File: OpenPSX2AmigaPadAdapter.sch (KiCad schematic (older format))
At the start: 26 parts, among them J1 TO_PS_PAD, J2 TO_AMI, J3 CONN_FTDI, J4 CONN_ICSP, Q1 BSS138, Q2 BSS138, Q3 BSS138, Q4 BSS138, U1 ATMEGA328P-AU, U2 LM1117-3.3, Y1 16Mhz

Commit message: Minor improvements
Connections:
- wire segments 140 -> 116

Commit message: Add cap for ATmega decoupling
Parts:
- added C2: 100n, symbol C
- renumbered C2 to C3, C3 to C6
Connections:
- wire segments 116 -> 118
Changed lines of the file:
@@
 $EndComp
 $Comp
-L C C2
+L C C3
 U 1 1 5D18D235
 P 3200 5450
-F 0 "C2" H 3225 5550 50  0000 L CNN
+F 0 "C3" H 3225 5550 50  0000 L CNN
 F 1 "10u" H 3225 5350 50  0000 L CNN
 F 2 "" H 3238 5300 50  0001 C CNN
@@
 	2000 5000 2000 5300
 Wire Wire Line
-	2000 5150 2300 5150
+	1650 5150 2300 5150
 Wire Wire Line
 	2600 5450 2600 5950
@@
 	2000 5600 2000 5800
 Wire Wire Line
-	2000 5800 3200 5800
+	1650 5800 3200 5800
 Wire Wire Line
 	3200 5800 3200 5600
@@
 	3200 2750 3950 2750
 $Comp
-L C_Small C3
+L C_Small C6
 U 1 1 5D197DBF
 P 4050 2750
-F 0 "C3" H 4060 2820 50  0000 L CNN
+F 0 "C6" H 4060 2820 50  0000 L CNN
 F 1 "100n" H 4060 2670 50  0000 L CNN
 F 2 "Capacitors_SMD:C_0805_HandSoldering" H 4050 2750 50  0001 C CNN
@@
 Wire Wire Line
 	9900 800  9900 900
+$Comp
+L C C2
+U 1 1 5D1A1AA9
+P 1650 5450
+F 0 "C2" H 1675 5550 50  0000 L CNN
+F 1 "100n" H 1675 5350 50  0000 L CNN
+F 2 "" H 1688 5300 50  0001 C CNN
+F 3 "" H 1650 5450 50  0001 C CNN
+	1    1650 5450
+	1    0    0    -1
+$EndComp
+Wire Wire Line
+	1650 5150 1650 5300
+Wire Wire Line
+	1650 5600 1650 5800
+Connection ~ 2000 5800
 $EndSCHEMATC

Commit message: Port to KiCad 5
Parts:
- removed C1, C3: 10u, symbol C
- removed C2: 100n, symbol C
- removed C4, C5: 22p, symbol C
- removed C6: 100n, Capacitors_SMD:C_0805_HandSoldering, symbol C_Small
- removed J1: TO_PS_PAD, symbol CONN_01X09
- removed J2: TO_AMI, symbol DB9_FEMALE_MountingHoles
- removed J3: CONN_FTDI, symbol CONN_01X06
- removed J4: CONN_ICSP, Pin_Headers:Pin_Header_Straight_2x03, symbol CONN_02X03
- removed Q1, Q2, Q3, Q4: BSS138, TO_SOT_Packages_SMD:SOT-23, symbol BSS138
- removed R1: 10k, Resistors_SMD:R_0805_HandSoldering, symbol R
- removed R10: 100, symbol R
- removed R2, R3, R4, R5, R6, R7, R8, R9: 10k, symbol R
- removed U1: ATMEGA328P-AU, TQFP32, symbol ATMEGA328P-AU
- removed U2: LM1117-3.3, symbol LM1117-3.3
- removed Y1: 16Mhz, symbol Crystal
- added C1, C2: 10u, Capacitor_SMD:C_1206_3216Metric_Pad1.42x1.75mm_HandSolder, symbol Device:C
- added C3, C4, C5, C8: 100n, Capacitor_SMD:C_0805_2012Metric_Pad1.15x1.40mm_HandSolder, symbol Device:C
- added C6, C7: 22p, Capacitor_SMD:C_0805_2012Metric_Pad1.15x1.40mm_HandSolder, symbol Device:C
- added D1, D2: LED, LED_SMD:LED_0805_2012Metric_Pad1.15x1.40mm_HandSolder, symbol Device:LED
- added J1: TO_PSX_PAD, Connector_PinHeader_2.54mm:PinHeader_1x09_P2.54mm_Horizontal, symbol Connector:Conn_01x09_Female
- added J2: TO_AMI, w_conn_d-sub:DB_9F, symbol Connector:DB9_Female_MountingHoles
- added J3: CONN_FTDI, Connector_PinSocket_2.54mm:PinSocket_1x06_P2.54mm_Vertical, symbol Connector:Conn_01x06_Male
- added J4: CONN_ICSP, Connector_PinSocket_2.54mm:PinSocket_2x03_P2.54mm_Vertical, symbol Connector_Generic:Conn_02x03_Odd_Even
- added Q1, Q2, Q3, Q4: BSS138, Package_TO_SOT_SMD:SOT-23, symbol Transistor_FET:BSS138
- added R1, R2, R3, R4, R5, R6, R7, R8, R9: 10k, Resistor_SMD:R_0805_2012Metric_Pad1.15x1.40mm_HandSolder, symbol Device:R
- added R10: 100, Resistor_SMD:R_0805_2012Metric_Pad1.15x1.40mm_HandSolder, symbol Device:R
- added R11: 220, Resistor_SMD:R_0805_2012Metric_Pad1.15x1.40mm_HandSolder, symbol Device:R
- added R220: R, Resistor_SMD:R_0805_2012Metric_Pad1.15x1.40mm_HandSolder, symbol Device:R
- added U1: ATmega328P-AU, Package_QFP:TQFP-32_7x7mm_P0.8mm, symbol MCU_Microchip_ATmega:ATmega328P-AU
- added U2: LM1117-3.3, Package_TO_SOT_SMD:SOT-223-3_TabPin2, symbol Regulator_Linear:LM1117-3.3
- added Y1: 16MHz, Crystal:Crystal_HC49-U_Vertical, symbol Device:Crystal
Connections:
- net labels added: led1, led2
- wire segments 118 -> 159
- no-connect marks 7 -> 11
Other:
- note added: "BOTH 10uF CAPS MUST\nPOSSIBLY BE TANTALUM"
- note removed: "BOTH CAPS MUST\nPOSSIBLY BE TANTALUM"

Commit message: Begin working on PCB
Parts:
- J1: footprint Connector_PinHeader_2.54mm:PinHeader_1x09_P2.54mm_Horizontal -> OpenPSX2AmigaPadAdapter:PSX_Pad_Connector
- J3: footprint Connector_PinSocket_2.54mm:PinSocket_1x06_P2.54mm_Vertical -> Connector_PinHeader_2.54mm:PinHeader_1x06_P2.54mm_Vertical
- J4: footprint Connector_PinSocket_2.54mm:PinSocket_2x03_P2.54mm_Vertical -> Connector_PinHeader_2.54mm:PinHeader_2x03_P2.54mm_Vertical
- R12: renamed from R220; value R -> 220
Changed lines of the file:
@@
 $EndComp
 Text Label 6600 7000 2    60   ~ 0
-miso
+mosi
 Text Label 5300 7100 0    60   ~ 0
 reset
@@
 F 0 "J1" H 9728 4826 50  0000 L CNN
 F 1 "TO_PSX_PAD" H 9728 4735 50  0000 L CNN
-F 2 "Connector_PinHeader_2.54mm:PinHeader_1x09_P2.54mm_Horizontal" H 9700 4800 50  0001 C CNN
+F 2 "OpenPSX2AmigaPadAdapter:PSX_Pad_Connector" H 9700 4800 50  0001 C CNN
 F 3 "~" H 9700 4800 50  0001 C CNN
 	1    9700 4800
@@
 F 0 "J4" H 5950 7317 50  0000 C CNN
 F 1 "CONN_ICSP" H 5950 7226 50  0000 C CNN
-F 2 "Connector_PinSocket_2.54mm:PinSocket_2x03_P2.54mm_Vertical" H 5900 7000 50  0001 C CNN
+F 2 "Connector_PinHeader_2.54mm:PinHeader_2x03_P2.54mm_Vertical" H 5900 7000 50  0001 C CNN
 F 3 "~" H 5900 7000 50  0001 C CNN
 	1    5900 7000
@@
 F 0 "J3" H 4008 7331 50  0000 C CNN
 F 1 "CONN_FTDI" H 4008 7240 50  0000 C CNN
-F 2 "Connector_PinSocket_2.54mm:PinSocket_1x06_P2.54mm_Vertical" H 3900 6950 50  0001 C CNN
+F 2 "Connector_PinHeader_2.54mm:PinHeader_1x06_P2.54mm_Vertical" H 3900 6950 50  0001 C CNN
 F 3 "~" H 3900 6950 50  0001 C CNN
 	1    3900 6950
@@
 $EndComp
 $Comp
-L Device:R R220
+L Device:R R12
 U 1 1 5D343E5C
 P 4340 5575
-F 0 "R220" V 4455 5575 50  0000 C CNN
-F 1 "R" V 4546 5575 50  0000 C CNN
+F 0 "R12" V 4455 5575 50  0000 C CNN
+F 1 "220" V 4546 5575 50  0000 C CNN
 F 2 "Resistor_SMD:R_0805_2012Metric_Pad1.15x1.40mm_HandSolder" V 4270 5575 50  0001 C CNN
 F 3 "~" H 4340 5575 50  0001 C CNN

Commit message: Ready?
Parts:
- added D1: 1n5817, Diode_SMD:D_SMA_Handsoldering, symbol Device:D
- added J99: OSHW_LOGO, Symbol:OSHW-Logo_5.7x6mm_Copper, symbol Connector:Conn_01x01_Male
- J2: footprint w_conn_d-sub:DB_9F -> OpenPSX2AmigaPadAdapter:DB_9F
- renumbered D1 to LD1, D2 to LD2
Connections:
- wire segments 159 -> 160
- no-connect marks 11 -> 12
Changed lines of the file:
@@
 encoding utf-8
 Sheet 1 1
-Title "MyTrackr"
-Date "2019-07-01"
-Rev "1"
+Title "OpenPSX2AmigaPadAdapter"
+Date "2019-07-03"
+Rev "1git"
 Comp "SukkoPera"
 Comment1 ""
@@
 L power:+5V #PWR09
 U 1 1 5D18D86C
-P 9250 1500
-F 0 "#PWR09" H 9250 1350 50  0001 C CNN
-F 1 "+5V" H 9250 1640 50  0000 C CNN
-F 2 "" H 9250 1500 50  0001 C CNN
-F 3 "" H 9250 1500 50  0001 C CNN
-	1    9250 1500
+P 9250 1300
+F 0 "#PWR09" H 9250 1150 50  0001 C CNN
+F 1 "+5V" H 9250 1440 50  0000 C CNN
+F 2 "" H 9250 1300 50  0001 C CNN
+F 3 "" H 9250 1300 50  0001 C CNN
+	1    9250 1300
 	1    0    0    -1
 $EndComp
@@
 	9250 2350 9350 2350
 Wire Wire Line
-	9250 2150 9250 1500
+	9250 2150 9250 1690
 Wire Wire Line
 	9500 4400 8550 4400
@@
 F 0 "J2" H 9830 2252 50  0000 L CNN
 F 1 "TO_AMI" H 9830 2161 50  0000 L CNN
-F 2 "w_conn_d-sub:DB_9F" H 9650 2250 50  0001 C CNN
+F 2 "OpenPSX2AmigaPadAdapter:DB_9F" H 9650 2250 50  0001 C CNN
 F 3 " ~" H 9650 2250 50  0001 C CNN
 	1    9650 2250
@@
 NoConn ~ 3200 2350
 $Comp
-L Device:LED D1
+L Device:LED LD1
 U 1 1 5D311FEE
 P 4775 5375
-F 0 "D1" H 4768 5120 50  0000 C CNN
-F 1 "LED" H 4768 5211 50  0000 C CNN
+F 0 "LD1" H 4768 5211 50  0000 C CNN
+F 1 "LED" H 4768 5211 50  0001 C CNN
 F 2 "LED_SMD:LED_0805_2012Metric_Pad1.15x1.40mm_HandSolder" H 4775 5375 50  0001 C CNN
 F 3 "~" H 4775 5375 50  0001 C CNN
@@
 $EndComp
 $Comp
-L Device:LED D2
+L Device:LED LD2
 U 1 1 5D332AA0
 P 4775 5575
-F 0 "D2" H 4768 5698 50  0000 C CNN
-F 1 "LED" H 4768 5789 50  0000 C CNN
+F 0 "LD2" H 4768 5699 50  0000 C CNN
+F 1 "LED" H 4768 5789 50  0001 C CNN
 F 2 "LED_SMD:LED_0805_2012Metric_Pad1.15x1.40mm_HandSolder" H 4775 5575 50  0001 C CNN
 F 3 "~" H 4775 5575 50  0001 C CNN
@@
 	2650 855  2700 855
 NoConn ~ 3200 1350
+Wire Wire Line
+	9250 1390 9250 1300
+$Comp
+L Device:D D1
+U 1 1 5D314735
+P 9250 1540
+F 0 "D1" V 9204 1619 50  0000 L CNN
+F 1 "1n5817" V 9295 1619 50  0000 L CNN
+F 2 "Diode_SMD:D_SMA_Handsoldering" H 9250 1540 50  0001 C CNN
+F 3 "~" H 9250 1540 50  0001 C CNN
+	1    9250 1540
+	0    1    1    0
+$EndComp
+$Comp
+L Connector:Conn_01x01_Male J99
+U 1 1 5D3ECFE7
+P 10625 6480
+F 0 "J99" V 10779 6392 50  0000 R CNN
+F 1 "OSHW_LOGO" V 10688 6392 50  0000 R CNN
+F 2 "Symbol:OSHW-Logo_5.7x6mm_Copper" H 10625 6480 50  0001 C CNN
+F 3 "~" H 10625 6480 50  0001 C CNN
+	1    10625 6480
+	0    -1   -1   0
+$EndComp
+NoConn ~ 10625 6280
 $EndSCHEMATC

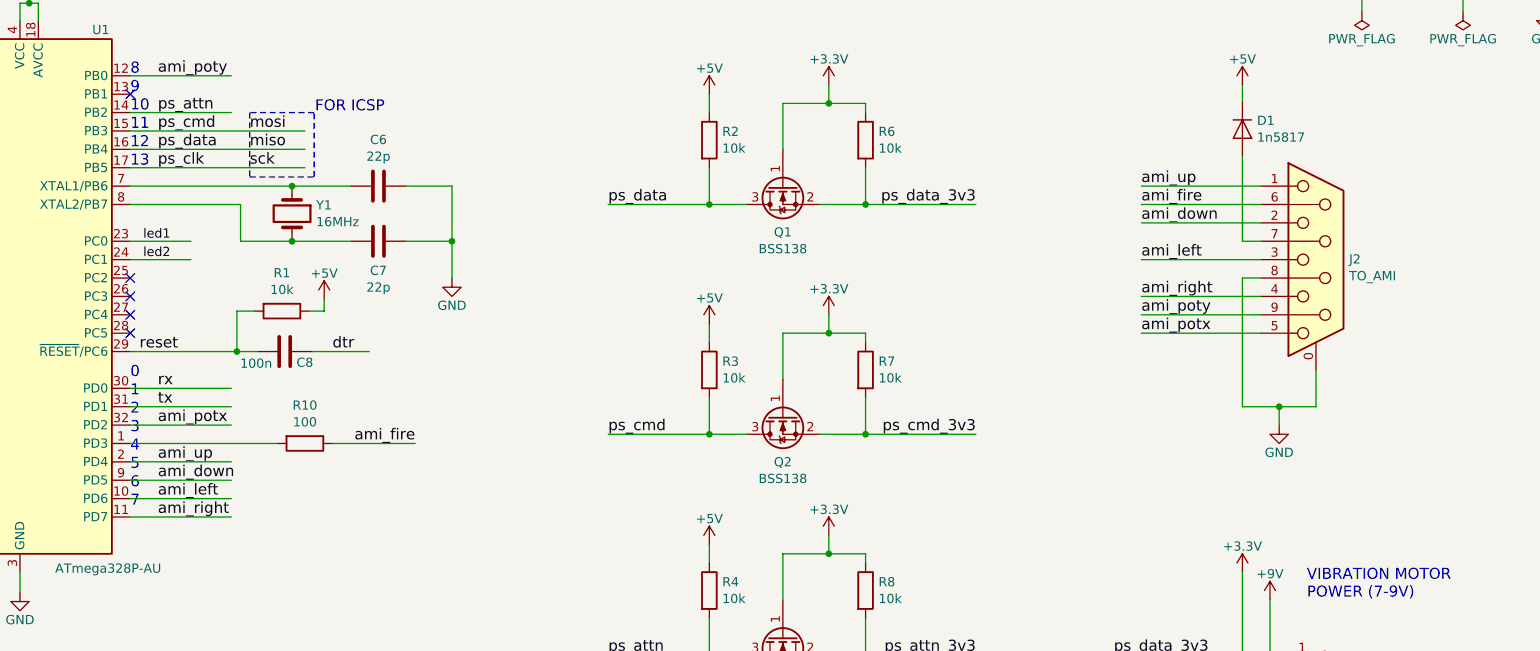
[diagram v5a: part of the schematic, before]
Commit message: Ready for V2 Added RESET button and lotsa minor adjustments
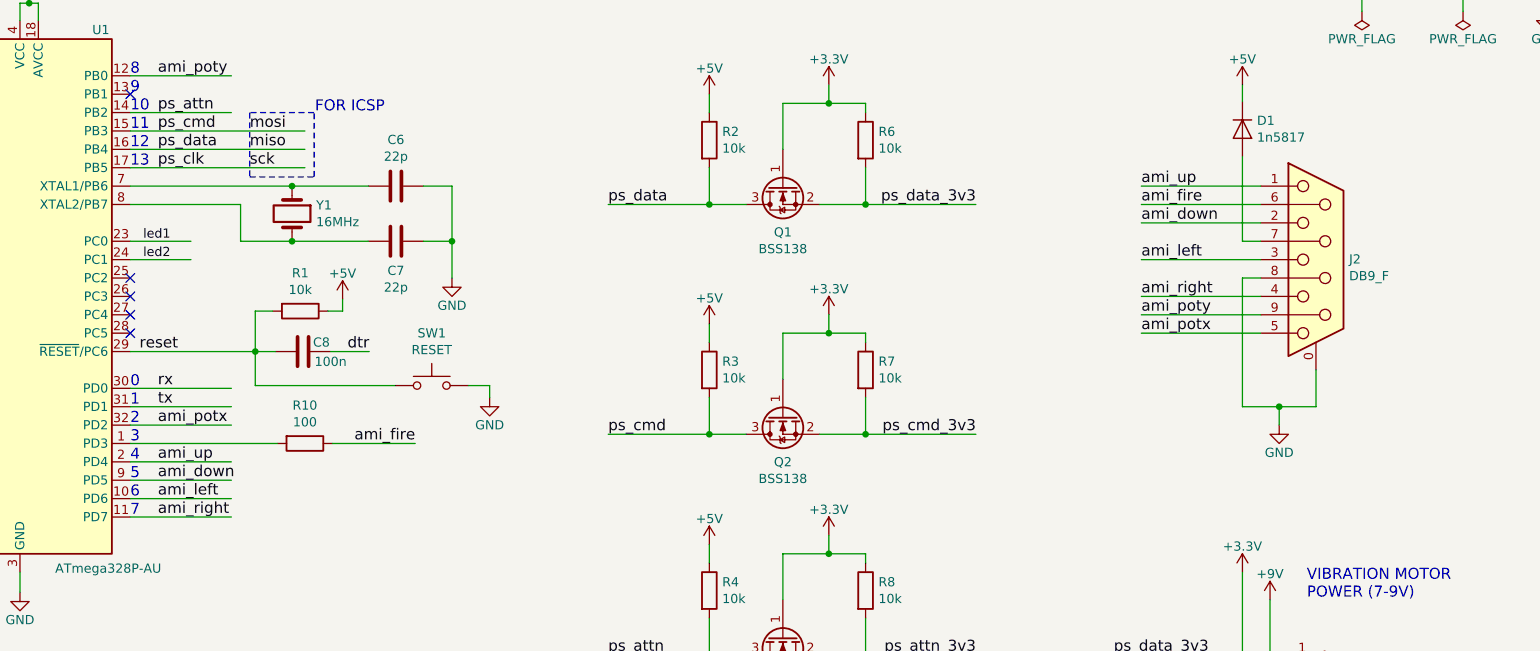
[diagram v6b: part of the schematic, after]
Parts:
- added SW1: RESET, Button_Switch_SMD:SW_SPST_EVPBF, symbol Switch:SW_Push
- D1: footprint Diode_SMD:D_SMA_Handsoldering -> Diode_SMD:D_SMA
- J2: value TO_AMI -> DB9_F
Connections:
- wire segments 160 -> 164
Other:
- moved on the sheet: C6, C7, C8, R1
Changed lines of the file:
@@
 Sheet 1 1
 Title "OpenPSX2AmigaPadAdapter"
-Date "2019-07-03"
+Date "2019-09-11"
 Rev "1git"
 Comp "SukkoPera"
@@
 Text Label 8700 2650 0    60   ~ 0
 ami_potx
-Text Notes 3200 2900 0    60   ~ 0
+Text Notes 3200 2950 0    60   ~ 0
 0
-Text Notes 3200 3000 0    60   ~ 0
+Text Notes 3200 3050 0    60   ~ 0
 1
-Text Notes 3200 3100 0    60   ~ 0
+Text Notes 3200 3150 0    60   ~ 0
 2
-Text Notes 3200 3200 0    60   ~ 0
+Text Notes 3200 3250 0    60   ~ 0
 3
-Text Notes 3200 3300 0    60   ~ 0
+Text Notes 3200 3350 0    60   ~ 0
 4
-Text Notes 3200 3400 0    60   ~ 0
+Text Notes 3200 3450 0    60   ~ 0
 5
-Text Notes 3200 3500 0    60   ~ 0
+Text Notes 3200 3550 0    60   ~ 0
 6
-Text Notes 3200 3600 0    60   ~ 0
+Text Notes 3200 3650 0    60   ~ 0
 7
 NoConn ~ 9500 5100
@@
 Text Label 5300 7000 0    60   ~ 0
 sck
-Text Label 4300 2750 0    60   ~ 0
+Text Label 4500 2750 2    60   ~ 0
 dtr
 Wire Wire Line
@@
 L power:+5V #PWR021
 U 1 1 5D197B2B
-P 4255 2465
-F 0 "#PWR021" H 4255 2315 50  0001 C CNN
-F 1 "+5V" H 4255 2605 50  0000 C CNN
-F 2 "" H 4255 2465 50  0001 C CNN
-F 3 "" H 4255 2465 50  0001 C CNN
-	1    4255 2465
+P 4355 2465
+F 0 "#PWR021" H 4355 2315 50  0001 C CNN
+F 1 "+5V" H 4355 2605 50  0000 C CNN
+F 2 "" H 4355 2465 50  0001 C CNN
+F 3 "" H 4355 2465 50  0001 C CNN
+	1    4355 2465
 	-1   0    0    -1
 $EndComp
@@
 L Device:R R1
 U 1 1 5D1B4196
-P 4025 2530
-F 0 "R1" V 3818 2530 50  0000 C CNN
-F 1 "10k" V 3909 2530 50  0000 C CNN
-F 2 "Resistor_SMD:R_0805_2012Metric_Pad1.15x1.40mm_HandSolder" V 3955 2530 50  0001 C CNN
-F 3 "~" H 4025 2530 50  0001 C CNN
-	1    4025 2530
+P 4125 2530
+F 0 "R1" V 3918 2530 50  0000 C CNN
+F 1 "10k" V 4009 2530 50  0000 C CNN
+F 2 "Resistor_SMD:R_0805_2012Metric_Pad1.15x1.40mm_HandSolder" V 4055 2530 50  0001 C CNN
+F 3 "~" H 4125 2530 50  0001 C CNN
+	1    4125 2530
 	0    1    1    0
 $EndComp
 Wire Wire Line
-	4190 2750 4500 2750
+	4290 2750 4500 2750
 $Comp
 L Device:R R2
@@
 P 9650 2250
 F 0 "J2" H 9830 2252 50  0000 L CNN
-F 1 "TO_AMI" H 9830 2161 50  0000 L CNN
+F 1 "DB9_F" H 9830 2161 50  0000 L CNN
 F 2 "OpenPSX2AmigaPadAdapter:DB_9F" H 9650 2250 50  0001 C CNN
 F 3 " ~" H 9650 2250 50  0001 C CNN
@@
 $EndComp
 Wire Wire Line
-	3875 2530 3780 2530
-Wire Wire Line
-	3780 2530 3780 2750
-Connection ~ 3780 2750
-Wire Wire Line
-	3780 2750 3890 2750
-Wire Wire Line
-	3200 2750 3780 2750
-Wire Wire Line
-	4255 2465 4255 2530
-Wire Wire Line
-	4255 2530 4175 2530
+	3975 2530 3880 2530
+Wire Wire Line
+	3880 2530 3880 2750
+Connection ~ 3880 2750
+Wire Wire Line
+	3880 2750 3990 2750
+Wire Wire Line
+	3200 2750 3880 2750
+Wire Wire Line
+	4355 2465 4355 2530
+Wire Wire Line
+	4355 2530 4275 2530
 $Comp
 L Device:C C8
 U 1 1 5D1C8DC2
-P 4040 2750
-F 0 "C8" V 4100 2860 50  0000 C CNN
-F 1 "100n" V 4105 2595 50  0000 C CNN
-F 2 "Capacitor_SMD:C_0805_2012Metric_Pad1.15x1.40mm_HandSolder" H 4078 2600 50  0001 C CNN
-F 3 "~" H 4040 2750 50  0001 C CNN
-	1    4040 2750
+P 4140 2750
+F 0 "C8" V 4090 2850 50  0000 C CNN
+F 1 "100n" V 4195 2900 50  0000 C CNN
+F 2 "Capacitor_SMD:C_0805_2012Metric_Pad1.15x1.40mm_HandSolder" H 4178 2600 50  0001 C CNN
+F 3 "~" H 4140 2750 50  0001 C CNN
+	1    4140 2750
 	0    1    1    0
 $EndComp
@@
 	3800 1950 3800 2150
 Wire Wire Line
-	4700 1850 4950 1850
+	4795 1850 4950 1850
 Wire Wire Line
 	4950 1850 4950 2150
@@
 L Device:C C6
 U 1 1 5D19A701
-P 4550 1850
-F 0 "C6" V 4298 1850 50  0000 C CNN
-F 1 "22p" V 4389 1850 50  0000 C CNN
-F 2 "Capacitor_SMD:C_0805_2012Metric_Pad1.15x1.40mm_HandSolder" H 4588 1700 50  0001 C CNN
-F 3 "~" H 4550 1850 50  0001 C CNN
-	1    4550 1850
+P 4645 1850
+F 0 "C6" V 4393 1850 50  0000 C CNN
+F 1 "22p" V 4484 1850 50  0000 C CNN
+F 2 "Capacitor_SMD:C_0805_2012Metric_Pad1.15x1.40mm_HandSolder" H 4683 1700 50  0001 C CNN
+F 3 "~" H 4645 1850 50  0001 C CNN
+	1    4645 1850
 	0    1    1    0
 $EndComp
@@
 $EndComp
 Wire Wire Line
-	4080 1850 4400 1850
+	4080 1850 4495 1850
 Connection ~ 4080 1850
 Wire Wire Line
@@
 ps_attn
 Wire Wire Line
-	4700 2150 4950 2150
+	4795 2150 4950 2150
 Wire Wire Line
 	4950 2150 4950 2350
@@
 L Device:C C7
 U 1 1 5D1A882F
-P 4550 2150
-F 0 "C7" V 4710 2150 50  0000 C CNN
-F 1 "22p" V 4801 2150 50  0000 C CNN
-F 2 "Capacitor_SMD:C_0805_2012Metric_Pad1.15x1.40mm_HandSolder" H 4588 2000 50  0001 C CNN
-F 3 "~" H 4550 2150 50  0001 C CNN
-	1    4550 2150
+P 4645 2150
+F 0 "C7" V 4805 2150 50  0000 C CNN
+F 1 "22p" V 4896 2150 50  0000 C CNN
+F 2 "Capacitor_SMD:C_0805_2012Metric_Pad1.15x1.40mm_HandSolder" H 4683 2000 50  0001 C CNN
+F 3 "~" H 4645 2150 50  0001 C CNN
+	1    4645 2150
 	0    1    1    0
 $EndComp
@@
 	3800 2150 4080 2150
 Wire Wire Line
-	4080 2150 4400 2150
+	4080 2150 4495 2150
 Connection ~ 4080 2150
 Connection ~ 4950 2150
@@
 F 0 "D1" V 9204 1619 50  0000 L CNN
 F 1 "1n5817" V 9295 1619 50  0000 L CNN
-F 2 "Diode_SMD:D_SMA_Handsoldering" H 9250 1540 50  0001 C CNN
+F 2 "Diode_SMD:D_SMA" H 9250 1540 50  0001 C CNN
 F 3 "~" H 9250 1540 50  0001 C CNN
 	1    9250 1540
@@
 $EndComp
 NoConn ~ 10625 6280
+$Comp
+L Switch:SW_Push SW1
+U 1 1 5D7A8F65
+P 4840 2935
+F 0 "SW1" H 4840 3220 50  0000 C CNN
+F 1 "RESET" H 4840 3129 50  0000 C CNN
+F 2 "Button_Switch_SMD:SW_SPST_EVPBF" H 4840 3135 50  0001 C CNN
+F 3 "~" H 4840 3135 50  0001 C CNN
+	1    4840 2935
+	1    0    0    -1
+$EndComp
+Wire Wire Line
+	3880 2750 3880 2935
+Wire Wire Line
+	3880 2935 4640 2935
+$Comp
+L power:GND #PWR028
+U 1 1 5D7B406A
+P 5155 3000
+F 0 "#PWR028" H 5155 2750 50  0001 C CNN
+F 1 "GND" H 5155 2850 50  0000 C CNN
+F 2 "" H 5155 3000 50  0001 C CNN
+F 3 "" H 5155 3000 50  0001 C CNN
+	1    5155 3000
+	1    0    0    -1
+$EndComp
+Wire Wire Line
+	5040 2935 5155 2935
+Wire Wire Line
+	5155 2935 5155 3000
 $EndSCHEMATC
